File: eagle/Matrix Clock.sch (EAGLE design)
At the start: 48 parts, among them IC1 MEGA32-A, IC2 LM1117IMPX-3.3, IC3 DS1307Z, IC4 MAX7219CWG, IC5 MAX7219CWG, IC6 MAX7219CWG, IC7 MAX7219CWG, Q1 32768, Q2 16MHz, X1 MINI-USB-SCHIELD-32005-301

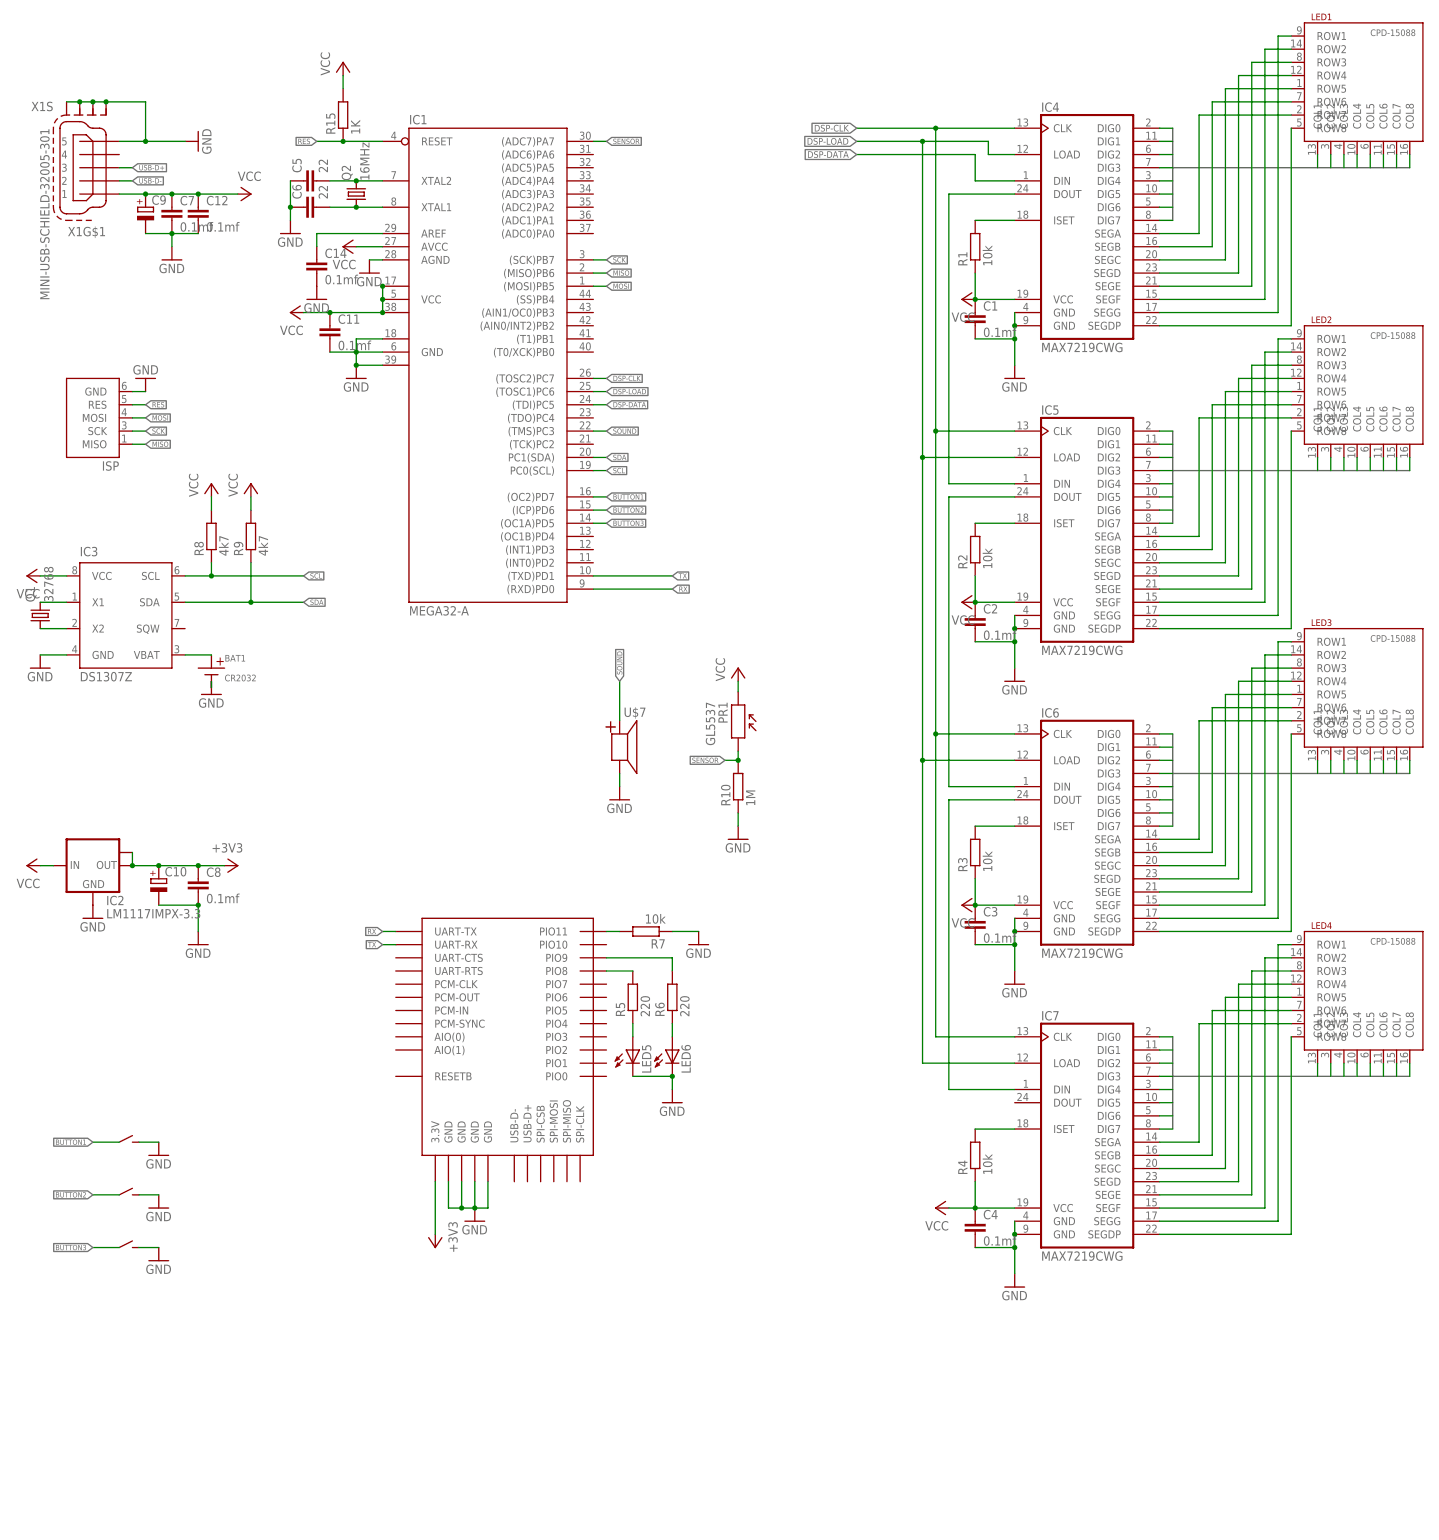
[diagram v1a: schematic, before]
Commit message: Big update
- Asyncronous USART operations
- Asyncronous ADC
- Updated schematics file and PCB
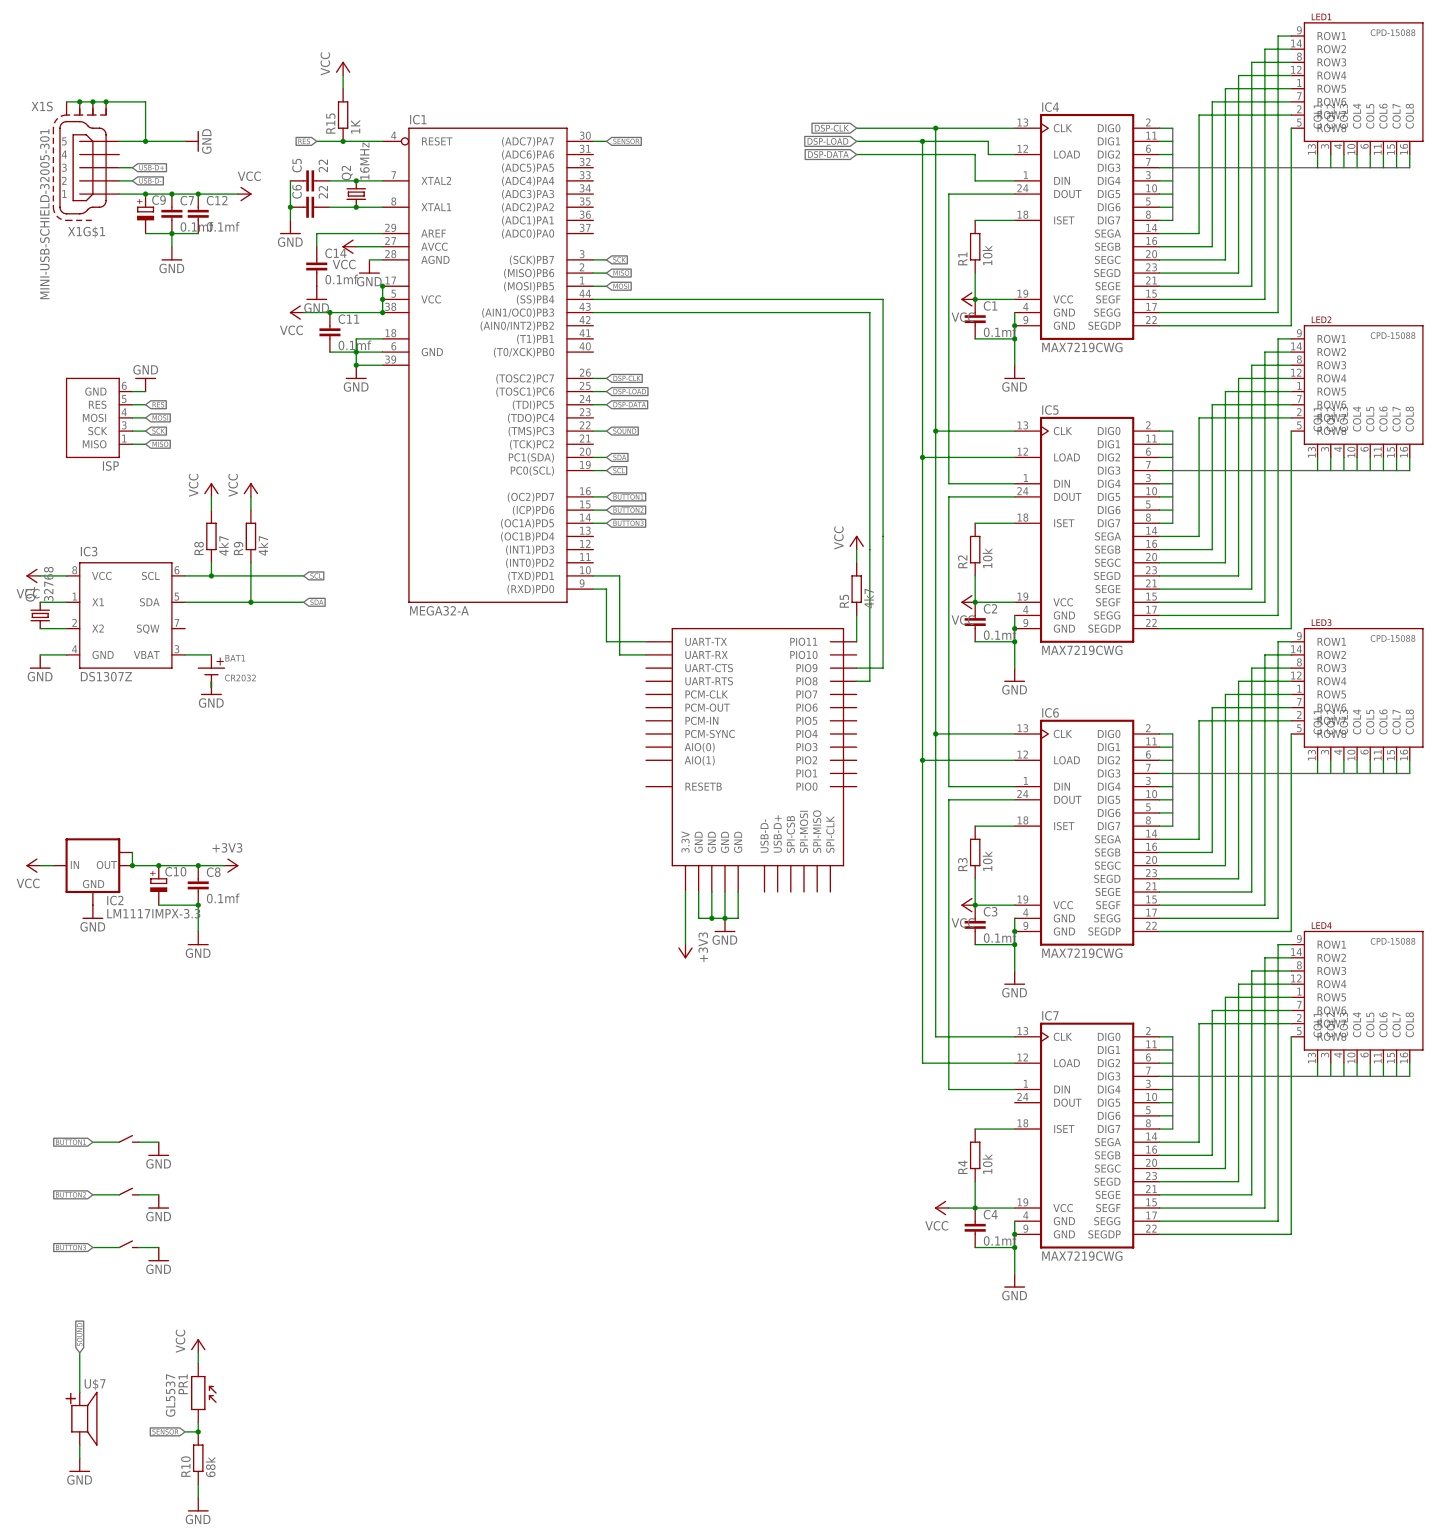
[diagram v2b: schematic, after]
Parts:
- removed LED5, LED6: (no value), LED:LEDSML1206
- removed R6: 220, rcl:R-EU_R0805
- removed R7: 10k, rcl:R-EU_R0805
- R10: value 1M -> 68k
- R5: value 220 -> 4k7
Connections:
- removed net RX: U$1.UART-TX
- removed net TX: U$1.UART-RX
- net GND: no longer LED5.C, LED6.C, R7.1
- net N$26: now also IC1.(SS)PB4, U$1.PIO9; no longer R5.2, U$1.PIO8
- net N$27: now also IC1.(AIN1/OC0)PB3, U$1.PIO8; no longer R6.2, U$1.PIO9
- net N$28: now also R5.1; no longer R7.2
- net N$4: now also IC1.(TXD)PD1, U$1.UART-RX; no longer LED6.A, R6.1
- net N$5: now also IC1.(RXD)PD0, U$1.UART-TX; no longer LED5.A, R5.1
- net VCC: now also R5.2
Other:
- moved on the sheet: PR1, R10, R5, U$7

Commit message: Updated schematics and board
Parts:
- removed IC2: LM1117IMPX-3.3, lm1117:LM1117IMPX-3.3
- added C13: 0.1mf, rcl:C-EUC0805
- added R11, R6, R7: 4k7, rcl:R-EU_R0805
- added U$2: LP2985AIM5-3.3, LP2985:LP2985AIM5-3.3
- C10: value (none) -> 0.1mf; device rcl:CPOL-EU153CLV-0405 -> rcl:C-EUC0805
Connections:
- new net BT_ENABLE: IC1.(AIN0/INT2)PB2, U$2.ON/OFF
- new net BYPASS: C13.1, U$2.BYPASS
- net +3V3: now also C10.1, U$2.VOUT; no longer C10.+, C8.1, IC2.OUT, IC2.OUT1
- net BUTTON1: now also IC1.(ADC0)PA0, R6.1; no longer IC1.(OC2)PD7
- net BUTTON2: now also IC1.(ADC1)PA1, R11.1; no longer IC1.(ICP)PD6
- net BUTTON3: now also IC1.(ADC2)PA2, R7.1
- net GND: now also C10.2, C13.2, U$2.GND; no longer C10.-, IC2.GND
- net SENSOR: now also C8.1
- net VCC: now also R11.2, R6.2, R7.2, U$2.VIN; no longer IC2.IN
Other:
- moved on the sheet: C8, PR1, R10, U$7

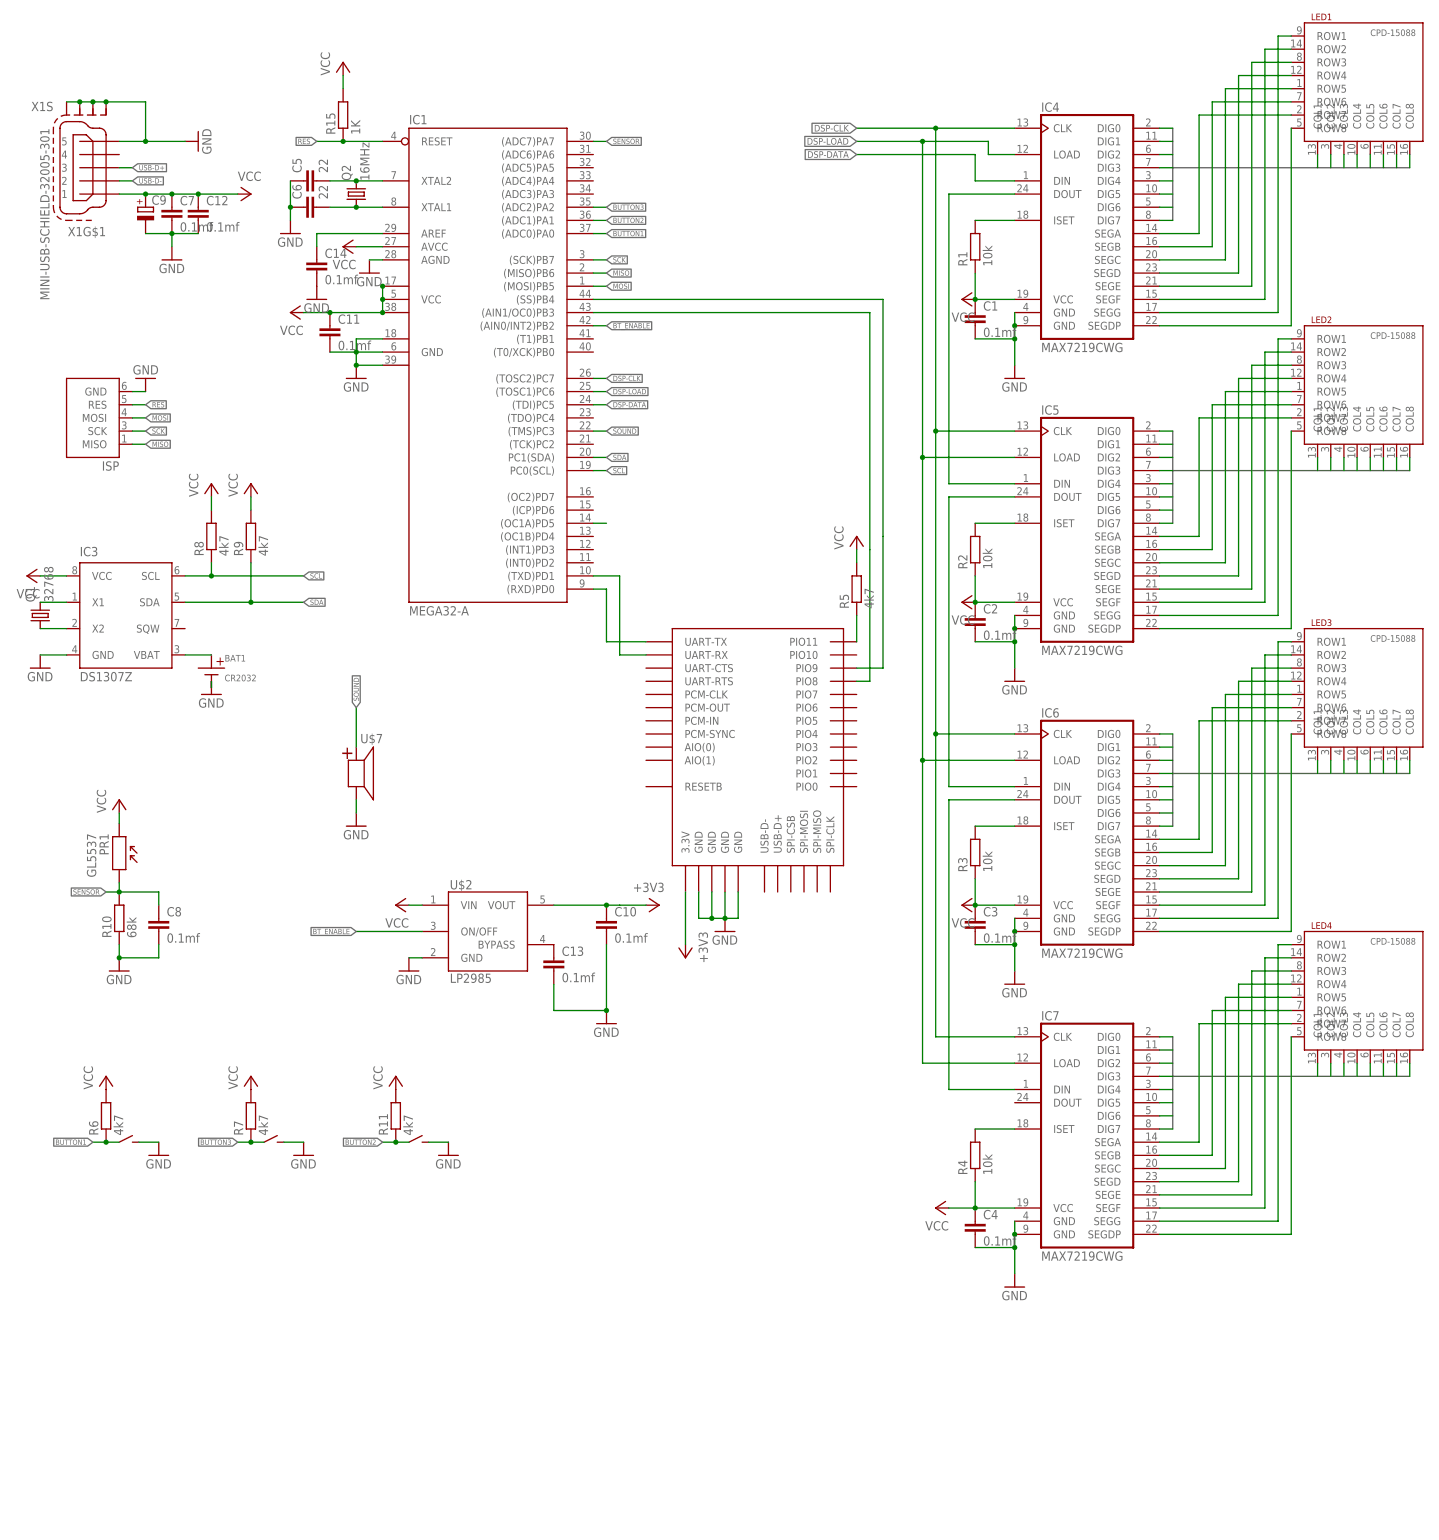
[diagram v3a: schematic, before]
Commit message: Removed outdated elements
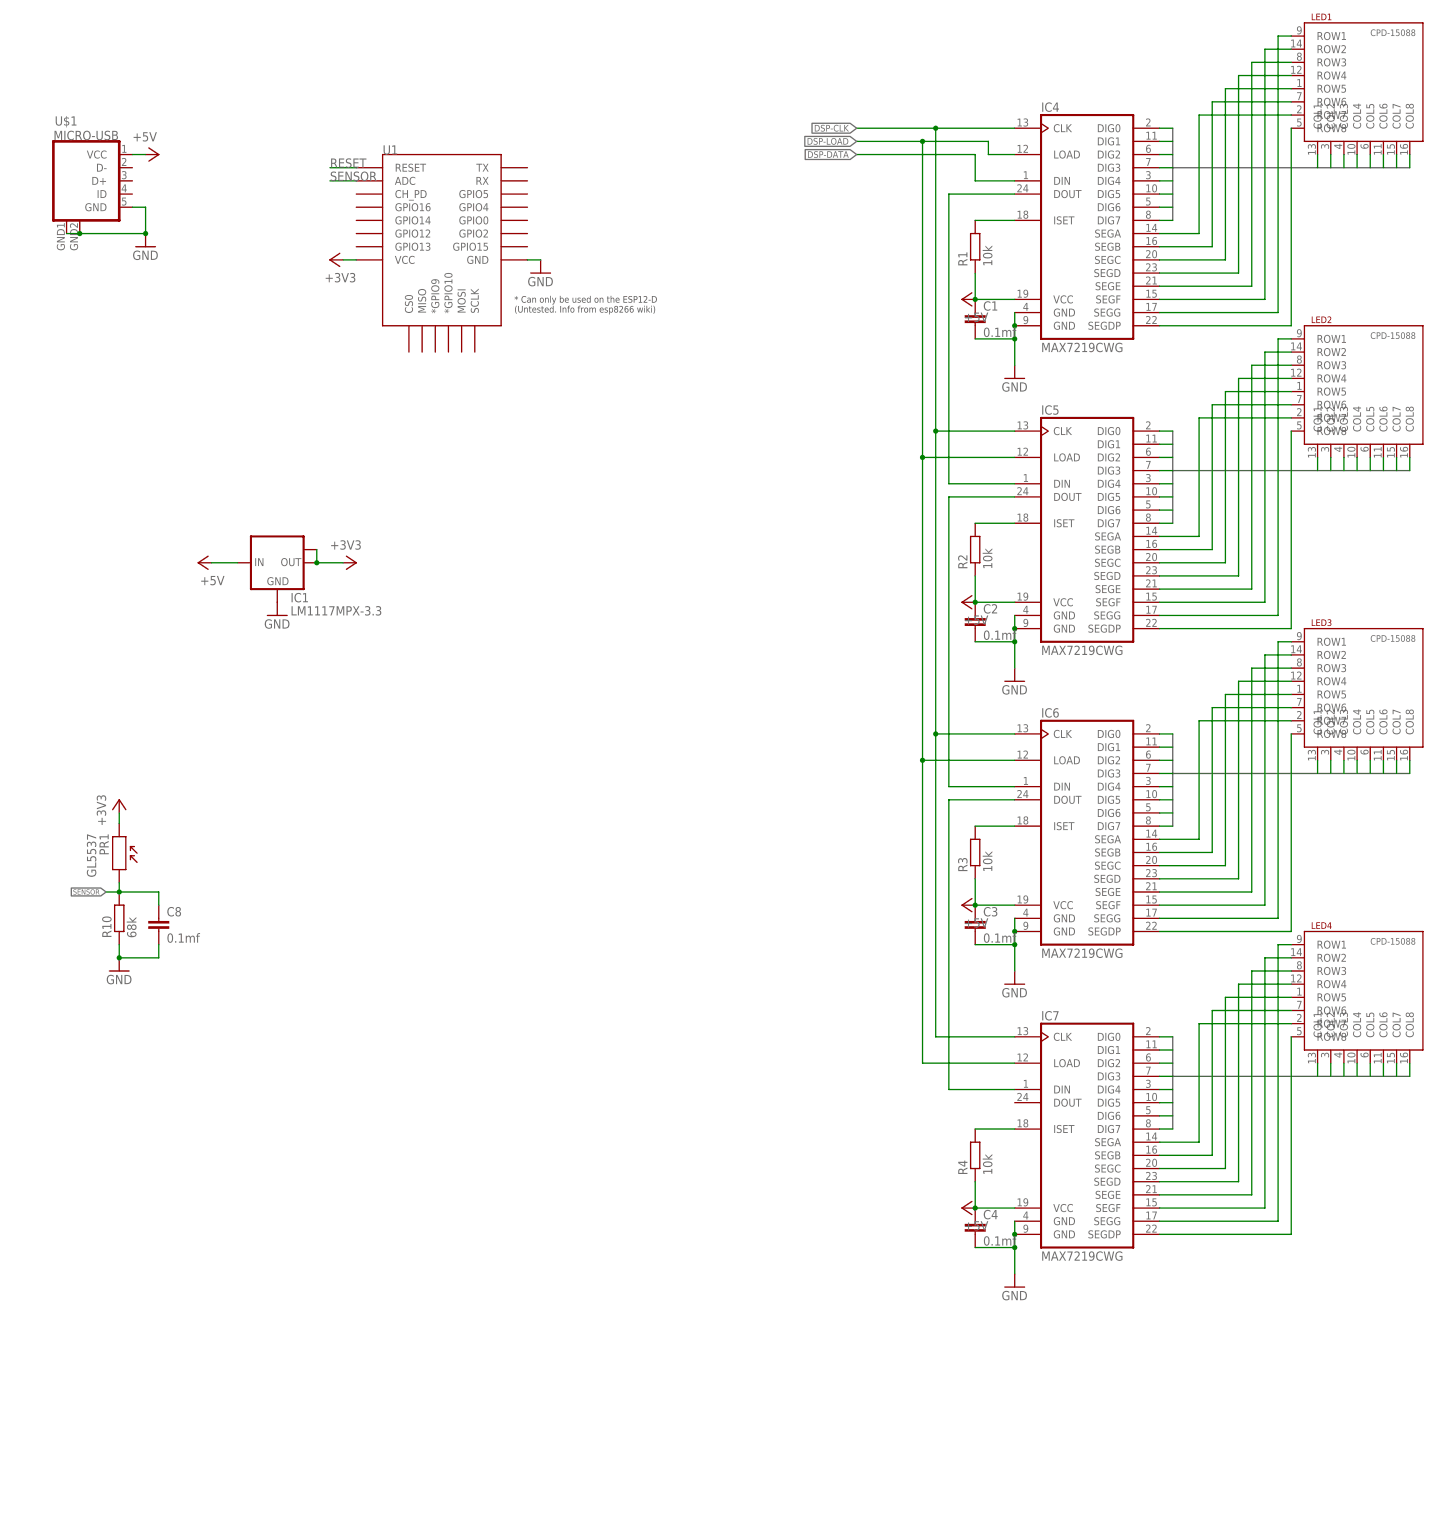
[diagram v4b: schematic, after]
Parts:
- removed BAT1: CR2032, misc:CR2032
- removed C10, C11, C12, C13, C14, C7: 0.1mf, rcl:C-EUC0805
- removed C5, C6: 22, rcl:C-EUC0805
- removed C9: (no value), rcl:CPOL-EU153CLV-0605
- removed IC3: DS1307Z, ds1307_pcf8583:DS1307Z
- removed Q1: 32768, crystal:CRYSTALTC38H
- removed Q2: 16MHz, crystal:CRYSTALHC49S
- removed R11, R5, R6, R7, R8, R9: 4k7, rcl:R-EU_R0805
- removed R15: 1K, rcl:R-EU_R0805
- removed U$10, U$11, U$9: IT1188E, misc:IT1188E
- removed U$2: LP2985AIM5-3.3, LP2985:LP2985AIM5-3.3
- removed U$3: AVR-ISP, misc:AVR-ISP
- removed U$7: HC0905, misc:HC0905
- removed X1: MINI-USB-SCHIELD-32005-301, con-cypressindustries:MINI-USB-SCHIELD-32005-301
- added U1: (no value), esp8266modules:ESP12ESMD
- IC1: value MEGA32-A -> LM1117MPX-3.3; device avr-7:MEGA32-A -> lm1117:LM1117MPX-3.3
- U$1: value (none) -> MICRO-USB; device bc417:BTM400_6B -> microusb:MICRO-USB
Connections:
- removed net BT_ENABLE: IC1.(AIN0/INT2)PB2, U$2.ON/OFF
- removed net BUTTON1: IC1.(ADC0)PA0, R6.1, U$9.3
- removed net BUTTON2: IC1.(ADC1)PA1, R11.1, U$10.3
- removed net BUTTON3: IC1.(ADC2)PA2, IC1.(OC1A)PD5, R7.1, U$11.3
- removed net BYPASS: C13.1, U$2.BYPASS
- removed net MISO: IC1.(MISO)PB6, U$3.MISO
- removed net MOSI: IC1.(MOSI)PB5, U$3.MOSI
- removed net N$26: IC1.(SS)PB4, U$1.PIO9
- removed net N$27: IC1.(AIN1/OC0)PB3, U$1.PIO8
- removed net N$28: R5.1, U$1.PIO11
- removed net N$3: BAT1.VBAT, IC3.VBAT
- removed net N$4: IC1.(TXD)PD1, U$1.UART-RX
- removed net N$5: IC1.(RXD)PD0, U$1.UART-TX
- removed net N$53: IC3.X1, Q1.2
- removed net N$54: IC3.X2, Q1.1
- removed net N$55: C14.1, IC1.AREF
- removed net RES: IC1.RESET, R15.1, U$3.RES
- removed net SCK: IC1.(SCK)PB7, U$3.SCK
- removed net SCL: IC1.PC0(SCL), IC3.SCL, R8.1
- removed net SDA: IC1.PC1(SDA), IC3.SDA, R9.1
- removed net SOUND: IC1.(TMS)PC3, U$7.P$2
- removed net USB-D+: X1G$1.3
- removed net USB-D-: X1G$1.2
- removed net VCC: C1.1, C11.1, C12.1, C2.1, C3.1, C4.1, C7.1, C9.+, IC1.AVCC, IC1.VCC, IC1.VCC1, IC1.VCC2, IC3.VCC, IC4.VCC, IC5.VCC, IC6.VCC, IC7.VCC, PR1.P$1, R1.1, R11.2, R15.2, R2.1, R3.1, R4.1, R5.2, R6.2, R7.2, R8.2, R9.2, U$2.VIN, X1G$1.1
- removed net XTAL1: C6.2, IC1.XTAL1, Q2.1
- removed net XTAL2: C5.2, IC1.XTAL2, Q2.2
- new net +5V: C1.1, C2.1, C3.1, C4.1, IC1.IN, IC4.VCC, IC5.VCC, IC6.VCC, IC7.VCC, R1.1, R2.1, R3.1, R4.1, U$1.VCC
- new net RESET: U1.RESET
- net +3V3: now also IC1.OUT, IC1.OUT1, PR1.P$1, U1.VCC; no longer C10.1, U$1.3.3V, U$2.VOUT
- net DSP-CLK: no longer IC1.(TOSC2)PC7
- net DSP-DATA: no longer IC1.(TDI)PC5
- net DSP-LOAD: no longer IC1.(TOSC1)PC6
- net GND: now also U$1.GND, U1.GND; no longer BAT1.GND, C10.2, C11.2, C12.2, C13.2, C14.2, C5.1, C6.1, C7.2, C9.-, IC1.AGND, IC1.GND1, IC1.GND2, IC3.GND, U$1.GND@3, U$1.GND@4, U$10.4, U$11.4, U$2.GND, U$3.GND, U$7.P$1, U$9.4, X1G$1.5, X1S.S1, X1S.S2, X1S.S3, X1S.S4
- net SENSOR: now also U1.ADC; no longer IC1.(ADC7)PA7
